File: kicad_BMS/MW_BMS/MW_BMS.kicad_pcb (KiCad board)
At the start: 4 copper layers, 51.3 x 46.2 mm, 82 parts, among them J1 Conn_01x02_Pin, J3 Conn_01x05_Pin, J4 Conn_01x02_Pin, Q1 CSD17578Q5A, Q3 NPN_BSS306NH6327XTSA1, Q4 PNP_BSS308PE, Q5 NPN_BSS306NH6327XTSA1, Q6 PNP_BSS308PE, T1 Transformer_1P_1S, U1 L9963E-TR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

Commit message: most_routing_done
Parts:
- CVCOM1: moved to F.Cu
- moved CNPN1 21.6 mm to (158.2, 98.0), turned to 0 degrees
- moved Q1 15.8 mm to (152.2, 98.0), turned to 90 degrees
- moved CBAT_2 14.6 mm to (158.2, 94.4)
- moved CBAT_1 14.4 mm to (158.4, 85.9)
- moved D1 13.6 mm to (157.9, 89.1)
- moved CESD1 10.8 mm to (163.2, 110.6)
- moved CESD2 10.8 mm to (163.2, 120.9)
- moved CBAT_3 10.8 mm to (158.2, 96.2)
- moved CISENSE_2 8.18 mm to (157.2, 109.5), turned to 0 degrees
- moved FR_BAT1 7.67 mm to (158.2, 92.2)
- moved CVCOM1 6.83 mm to (135.1, 95.9)
- moved CFIL2 6.12 mm to (138.3, 108.9), turned to 0 degrees
- moved CLPF3 5.72 mm to (156.9, 98.7), turned to -90 degrees
- moved CISENSE_3 5.61 mm to (157.2, 111.0), turned to 0 degrees
- moved CESD_4 5.50 mm to (164.2, 99.1)
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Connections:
- RSENSE_Shunt1 pad 1: /BATT_Minus -> /Cell1_minus
- RSENSE_Shunt1 pad 2: /Cell1_minus -> /BATT_Minus
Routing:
- net /CELL2_plus: track 0.00 -> 75.5 mm, vias 0 -> 1
- net /BATT_Plus: track 0.00 -> 62.6 mm, vias 0 -> 4
- net /VTREF: track 0.00 -> 37.5 mm, vias 0 -> 3
- net /S2: track 0.00 -> 36.7 mm, vias 0 -> 2
- net /VCOM: track 0.00 -> 34.3 mm, vias 0 -> 1
- net /B2_1: track 0.00 -> 30.6 mm, vias 0 -> 3
- net /S1: track 0.00 -> 29.3 mm, vias 0 -> 2
- net /S13: track 0.00 -> 27.1 mm, vias 0 -> 2
- net /ISENSEp: track 0.00 -> 26.9 mm
- net /B10_9: track 0.00 -> 21.9 mm, vias 0 -> 1
- net /ISENSEm: track 0.00 -> 19.2 mm
- net /C14: track 0.00 -> 18.4 mm
- net /C13: track 0.00 -> 17.6 mm
- net /ISOLm_NCS: track 0.00 -> 17.4 mm, vias 0 -> 1
- net /C12: track 0.00 -> 16.3 mm
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- added copper zone on B.Cu, net /VBAT

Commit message: more_improvements
just need ground planes, and to make a decision about cell3_minus
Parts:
- moved RFAULT1 2.53 mm to (134.6, 98.4)
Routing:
- net /B14_13: track 14.5 -> 39.0 mm, vias 2 -> 4
- net /VREG: track 2.74 -> 13.3 mm
- net GNDD: track 0.00 -> 7.86 mm, vias 0 -> 2
- net /GPIO2_ FAULTL: track 0.00 -> 7.52 mm
- net /ISOLp_SDI: track 14.6 -> 16.0 mm
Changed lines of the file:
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@@
 	(footprint "Resistor_SMD:R_0603_1608Metric"
 		(layer "F.Cu")
-		(at 135.875 100.6)
+		(at 134.625 98.4)
 		(descr "Resistor SMD 0603 (1608 Metric), square (rectangular) end terminal, IPC_7351 nominal, (Body size source: IPC-SM-782 page 72, https://www.pcb-3d.com/wordpress/wp-content/uploads/ipc-sm-782a_amendment_1_and_2.pdf), generated with kicad-footprint-generator")
 		(tags "resistor")
@@
 	)
 	(segment
+		(start 167.85 98.95)
+		(end 169.65 98.95)
+		(width 0.2)
+		(layer "F.Cu")
+		(net "/B14_13")
+	)
+	(segment
 		(start 146.811599 92.411599)
 		(end 146.372785 92.850412)
@@
 	)
 	(segment
+		(start 169.65 98.95)
+		(end 169.7 98.9)
+		(width 0.2)
+		(layer "F.Cu")
+		(net "/B14_13")
+	)
+	(segment
 		(start 167.85 98.95)
 		(end 167.05 98.95)
@@
 	)
 	(via
+		(at 154 88.9)
+		(size 0.6)
+		(drill 0.3)
+		(layers "F.Cu" "B.Cu")
+		(net "/B14_13")
+	)
+	(via
+		(at 169.7 98.9)
+		(size 0.6)
+		(drill 0.3)
+		(layers "F.Cu" "B.Cu")
+		(net "/B14_13")
+	)
+	(via
 		(at 150.2 89)
 		(size 0.4)
@@
 	)
 	(segment
+		(start 169.7 94.2)
+		(end 164.4 88.9)
+		(width 0.2)
+		(layer "In2.Cu")
+		(net "/B14_13")
+	)
+	(segment
+		(start 164.4 88.9)
+		(end 154 88.9)
+		(width 0.2)
+		(layer "In2.Cu")
+		(net "/B14_13")
+	)
+	(segment
 		(start 150.2 89.023197)
 		(end 150.2 89)
@@
 	)
 	(segment
+		(start 169.7 98.9)
+		(end 169.7 94.2)
+		(width 0.2)
+		(layer "In2.Cu")
+		(net "/B14_13")
+	)
+	(segment
 		(start 150.4 107.7)
 		(end 155.2 107.7)
@@
 	)
 	(segment
+		(start 143.7 91.6)
+		(end 143.7 92.3)
+		(width 0.3)
+		(layer "B.Cu")
+		(net "/ISOLp_SDI")
+	)
+	(segment
 		(start 145.4 89.7)
 		(end 145.4 89.3)
@@
 	)
 	(segment
+		(start 143.7 92.3)
+		(end 143.2 92.8)
+		(width 0.3)
+		(layer "B.Cu")
+		(net "/ISOLp_SDI")
+	)
+	(segment
 		(start 145.4 86.9)
 		(end 145.4 89.3)
@@
 	)
 	(segment
+		(start 133.8 99.5)
+		(end 133.8 98.4)
+		(width 0.2)
+		(layer "F.Cu")
+		(net "GNDD")
+	)
+	(segment
+		(start 127.7 101.1)
+		(end 129.2 101.1)
+		(width 0.2)
+		(layer "F.Cu")
+		(net "GNDD")
+	)
+	(via
+		(at 129.2 101.1)
+		(size 0.4)
+		(drill 0.2)
+		(layers "F.Cu" "B.Cu")
+		(net "GNDD")
+	)
+	(via
+		(at 133.8 99.5)
+		(size 0.4)
+		(drill 0.2)
+		(layers "F.Cu" "B.Cu")
+		(net "GNDD")
+	)
+	(segment
+		(start 132.2 101.1)
+		(end 133.8 99.5)
+		(width 0.2)
+		(layer "In2.Cu")
+		(net "GNDD")
+	)
+	(segment
+		(start 129.2 101.1)
+		(end 132.2 101.1)
+		(width 0.2)
+		(layer "In2.Cu")
+		(net "GNDD")
+	)
+	(segment
 		(start 141.9462 99.099622)
 		(end 141.9462 98.599496)
@@
 	)
 	(segment
-		(start 141.9462 101.100126)
-		(end 140.700126 101.100126)
+		(start 141.2 100.6)
+		(end 138.85 98.25)
+		(width 0.2)
+		(layer "F.Cu")
+		(net "/GPIO2_ FAULTL")
+	)
+	(segment
+		(start 138.85 98.25)
+		(end 135.4 98.25)
+		(width 0.2)
+		(layer "F.Cu")
+		(net "/GPIO2_ FAULTL")
+	)
+	(segment
+		(start 141.9462 100.6)
+		(end 141.2 100.6)
+		(width 0.2)
+		(layer "F.Cu")
+		(net "/GPIO2_ FAULTL")
+	)
+	(segment
+		(start 140.200126 101.100126)
+		(end 138.5 99.4)
 		(width 0.2)
 		(layer "F.Cu")
@@
 	)
 	(segment
-		(start 140.700126 101.100126)
+		(start 138.5 99.4)
 		(end 138.5 98.9)
 		(width 0.2)
@@
 		(net "/GPIO3")
 	)
+	(segment
+		(start 141.9462 101.100126)
+		(end 140.200126 101.100126)
+		(width 0.2)
+		(layer "F.Cu")
+		(net "/GPIO3")
+	)
 	(via
 		(at 138.5 98.9)
@@
 	)
 	(segment
+		(start 144.5 106)
+		(end 144.2 105.7)
+		(width 0.2)
+		(layer "B.Cu")
+		(net "/VREG")
+	)
+	(segment
+		(start 151.565 100.655)
+		(end 151.565 102.042107)
+		(width 0.2)
+		(layer "B.Cu")
+		(net "/VREG")
+	)
+	(segment
+		(start 151.565 102.042107)
+		(end 147.607107 106)
+		(width 0.2)
+		(layer "B.Cu")
+		(net "/VREG")
+	)
+	(segment
 		(start 144.2 106.7)
 		(end 144.2 105.7)
 		(width 0.2)
 		(layer "B.Cu")
+		(net "/VREG")
+	)
+	(segment
+		(start 147.607107 106)
+		(end 144.5 106)
+		(width 0.2)
+		(layer "B.Cu")

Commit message: updates
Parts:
- added NT1: NetTie_3, NetTie:NetTie-3_THT_Pad1.0mm, F.Cu at (147.7, 89.6)
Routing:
- net /B14_13: track 39.0 -> 47.3 mm, vias 4 -> 3
- net /CELL2_plus: track 75.5 -> 76.5 mm
- added copper zone on In2.Cu, net (none)
- added copper zone on F.Cu, net GNDA
- added copper zone on B.Cu, net GNDD

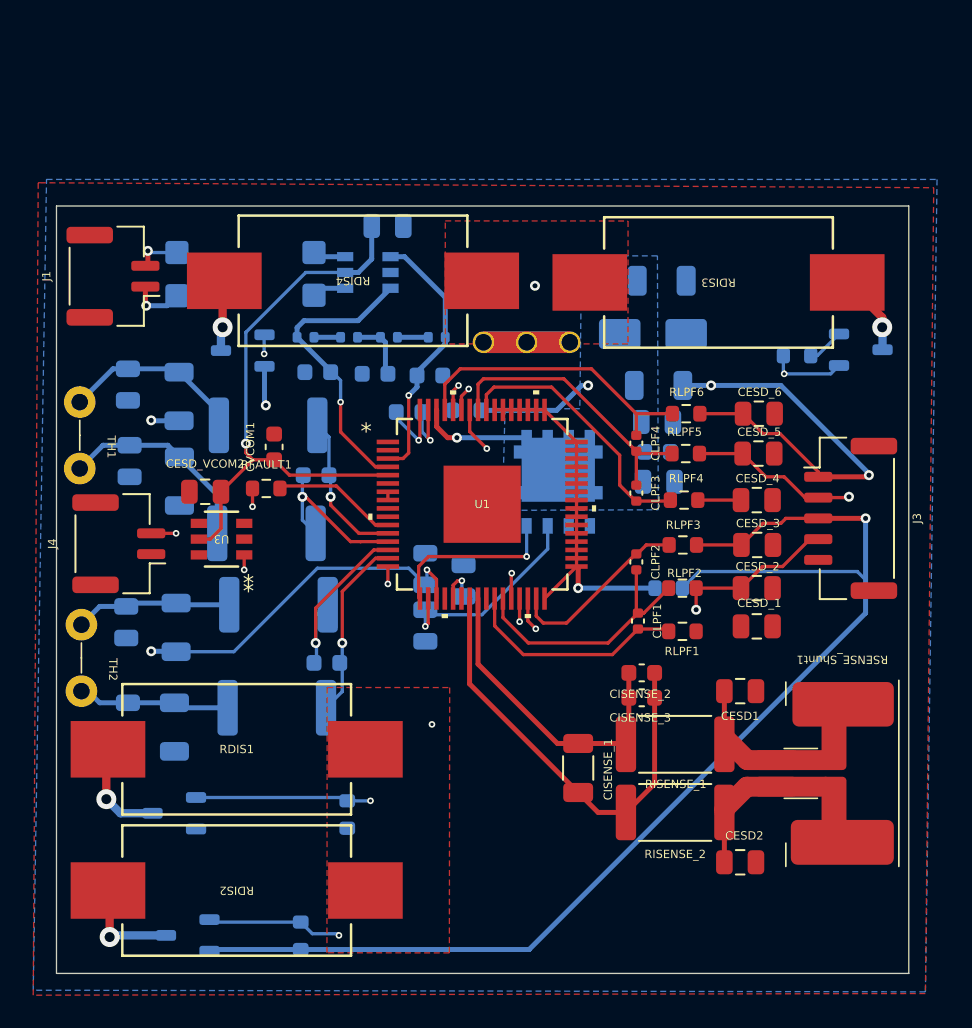
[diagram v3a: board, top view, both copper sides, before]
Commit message: fixed spi
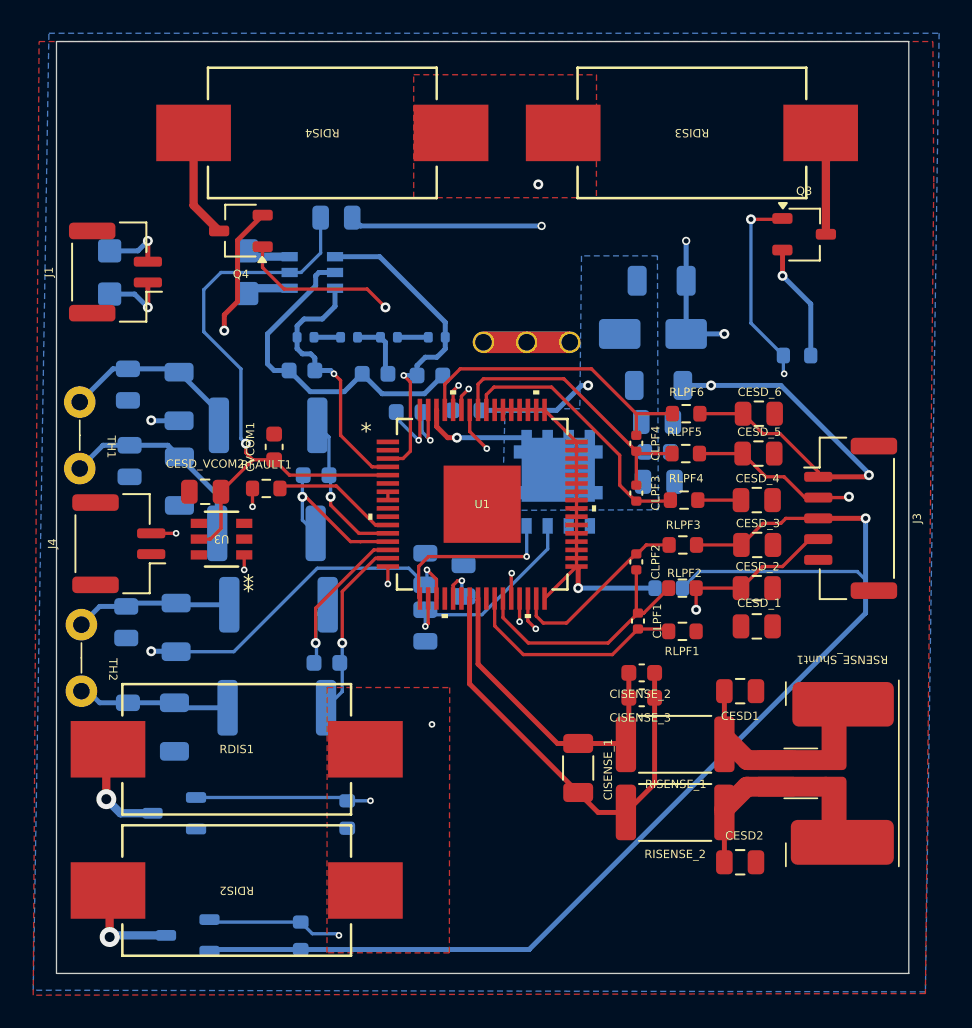
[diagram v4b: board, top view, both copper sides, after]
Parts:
- Q3, Q4: moved to F.Cu
- moved RDIS3 9.14 mm to (160.2, 77.0)
- moved RDIS4 9.09 mm to (138.0, 77.0)
- moved Q3 7.74 mm to (167.0, 83.1)
- moved Q4 7.20 mm to (133.1, 82.9)
- moved T1 4.05 mm to (129.3, 85.4)
- moved U2 3.34 mm to (137.4, 85.4)
- moved CESD_VCOM1 3.12 mm to (138.8, 82.1)
- moved CCM_MHZ2 0.96 mm to (136.8, 91.3)
- moved J1 0.29 mm to (125.5, 85.4)
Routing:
- net GNDD: track 7.86 -> 28.3 mm
- net GND_ESD: track 0.00 -> 19.5 mm, vias 0 -> 3
- net /BATT_Plus: track 62.6 -> 73.6 mm
- net /B14_13: track 47.3 -> 55.5 mm
- net /S13: track 27.1 -> 34.6 mm, vias 2 -> 3
- net /CELL3_minus: track 4.84 -> 9.66 mm, vias 0 -> 1
- net /ISOLp_SDI: track 16.0 -> 19.6 mm
- net /S14: track 15.3 -> 18.6 mm
- net /VCOM: track 34.3 -> 36.6 mm
- net Net-(Q4-D): track 4.28 -> 6.54 mm, vias 1 -> 0
- net Net-(J1-Pin_2): track 2.75 -> 4.51 mm
- net Net-(Q3-S): track 4.93 -> 6.23 mm, vias 1 -> 0
- net /ISOLm_NCS: track 17.4 -> 16.1 mm
- net Net-(J1-Pin_1): track 3.27 -> 4.13 mm
- net Net-(T1-AA): track 1.98 -> 2.73 mm
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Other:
- board size 51.3 x 46.2 mm -> 51.3 x 56.1 mm

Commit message: ground connected
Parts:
- moved CESD_6 0.83 mm to (163.4, 93.9)
- moved CESD_5 0.80 mm to (163.4, 96.3)
- moved CESD_1 0.76 mm to (163.4, 107.0)
- moved CESD_3 0.73 mm to (163.4, 101.8)
- moved CESD_2 0.70 mm to (163.4, 104.4)
- moved CESD_4 0.70 mm to (163.4, 99.1)
- moved RLPF6 0.22 mm to (159.7, 93.9)
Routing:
- net GND_ESD: track 19.5 -> 78.8 mm, vias 3 -> 16
- net GNDA: track 0.00 -> 30.6 mm, vias 0 -> 7
- net /CELL3_minus: track 9.66 -> 8.96 mm
